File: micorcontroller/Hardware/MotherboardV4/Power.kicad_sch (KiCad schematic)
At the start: 57 parts, among them J0 MS3112E8-4P

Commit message: propper Serial Comand System added
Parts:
- added BuckJmp0: Conn_01x03, Connector_PinHeader_2.54mm:PinHeader_1x03_P2.54mm_Vertical, symbol Connector_Generic:Conn_01x03
- C11: value 12p -> DNP; footprint Capacitor_SMD:C_0805_2012Metric_Pad1.18x1.45mm_HandSolder -> Capacitor_SMD:C_0402_1005Metric_Pad0.74x0.62mm_HandSolder
- C15: value 10u -> DNP
- C18: value 22u -> DNP
- LRlan0, LRre0, LRuC0: footprint SOT230P700X180-4N -> SamacSys_Parts:SOT230P700X180-4N
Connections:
- net +28V: now also BuckJmp0.2 (Pin_2); no longer C12.2, OP0.8 (V+)
- net 3V3_rest: now also C12.2, OP0.8 (V+)
- net GND: now also BuckJmp0.1 (Pin_1)
- net VBuck: now also BuckJmp0.3 (Pin_3)
- net RT: now reaches BUCK0.1 (RT), R11.1
- net SW: now reaches BUCK0.5 (SW), L0.1
- net SW: now also C10.1; no longer C10.2
- net BST: now reaches BUCK0.6 (BST), R14.1
- net SS: now reaches BUCK0.7 (SS), C9.2
- net FB: now reaches BUCK0.8 (FB), C11.2, R15.1, R16.2
- net at R14.2: now also C10.2; no longer C10.1
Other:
- moved on the sheet: C10, C11, C9, L0, R11, R14, R15, R16

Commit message: added a serial command field for easy debugging
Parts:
- removed R1: 12k, Resistor_SMD:R_0603_1608Metric_Pad0.98x0.95mm_HandSolder, symbol Device:R_Small
- added C76, C77: DNP, Capacitor_SMD:C_1210_3225Metric_Pad1.33x2.70mm_HandSolder, symbol Device:C
- C14: value 10u -> 10u/30V
- C17: value 0.1u -> 0.1u/30V
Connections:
- net +28V: now also C76.2
- net GND: now also C76.1, C77.1
- net VBuck: now also C77.2
- net at !bat0.1 (K), R0.1: now also bat0.2 (A)
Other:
- moved on the sheet: BUCK0, BuckJmp0, C10, C11, C13, C14, C15, C16, C17, C18, C9, L0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

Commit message: Switch to header BASED C file system {headache incomming}
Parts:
- removed C18: DNP, Capacitor_SMD:C_0805_2012Metric_Pad1.18x1.45mm_HandSolder, symbol Device:C
- C10: renamed from C76; footprint Capacitor_SMD:C_1210_3225Metric_Pad1.33x2.70mm_HandSolder -> Capacitor_SMD:C_0805_2012Metric_Pad1.18x1.45mm_HandSolder
- C20: renamed from C77; footprint Capacitor_SMD:C_1210_3225Metric_Pad1.33x2.70mm_HandSolder -> Capacitor_SMD:C_0805_2012Metric_Pad1.18x1.45mm_HandSolder
- renumbered C15 to C11, C17 to C12, C9 to C13, C12 to C14, C10 to C15, C11 to C16, C13 to C17, C16 to C18, C14 to C8, C8 to C9, L0 to L1, R2 to R1, R12 to R10, R13 to R12, R14 to R13, R15 to R14, R16 to R15, R3 to R2, R4 to R3, R5 to R4, R6 to R5, R7 to R6, R8 to R7, R9 to R8, R10 to R9
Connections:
- net VBuck renamed VBUCK
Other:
- moved on the sheet: C12, C20

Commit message: startup message
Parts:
- C3: value 0.22uF -> 1u
- C7: value 0.1u -> 1u
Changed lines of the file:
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@@
 			)
 		)
-		(property "Value" "0.1u"
+		(property "Value" "1u"
 			(at 68.58 162.5599 0)
 			(effects
@@
 			)
 		)
-		(property "Value" "0.22uF"
+		(property "Value" "1u"
 			(at 33.274 162.306 0)
 			(effects

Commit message: added uplink
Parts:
- !bat0, 5ext0, 5sys0, bat0, lan0, uC0: symbol Device:LED -> SymbolsBalloonv4:LED
- BT0: symbol Device:Battery_Cell -> SymbolsBalloonv4:Battery_Cell
- BUCK0: symbol SamacSys_Parts:TPS62933DRLR -> SymbolsBalloonv4:TPS62933DRLR
- BuckJmp0, JB_or_U0: symbol Connector_Generic:Conn_01x03 -> SymbolsBalloonv4:Conn_01x03
- C0, C1, C10, C11, C12, C13, C14, C15, C16, C17, C18, C2, C20, C4, C5, C6, C7, C8, C9: symbol Device:C -> SymbolsBalloonv4:C
- C3: value 1u -> 4.7u; symbol Device:C -> SymbolsBalloonv4:C
- D0, D1, D2: symbol Device:D_Zener -> SymbolsBalloonv4:D_Zener
- J0: symbol Connector:DIN-4 -> SymbolsBalloonv4:DIN-4
- L1: symbol Device:L_Small -> SymbolsBalloonv4:L_Small
- LR5V0: symbol SamacSys_Parts:MCP1826S-5002E_DB -> SymbolsBalloonv4:MCP1826S-5002E_DB
- LRlan0, LRre0, LRuC0: symbol SamacSys_Parts:NCP1117ST33T3G -> SymbolsBalloonv4:NCP1117ST33T3G
- OP0: symbol Device:Opamp_Dual -> SymbolsBalloonv4:Opamp_Dual
- R0, R1, R10, R11, R12, R13, R14, R15, R2, R3, R4, R5, R6, R7, R8, R9: symbol Device:R_Small -> SymbolsBalloonv4:R_Small
- R_shunt0: symbol SamacSys_Parts:PA1206FRE7W0R001Z -> SymbolsBalloonv4:PA1206FRE7W0R001Z
- V_BAT0: symbol Connector:Conn_01x04_Socket -> SymbolsBalloonv4:Conn_01x04_Socket

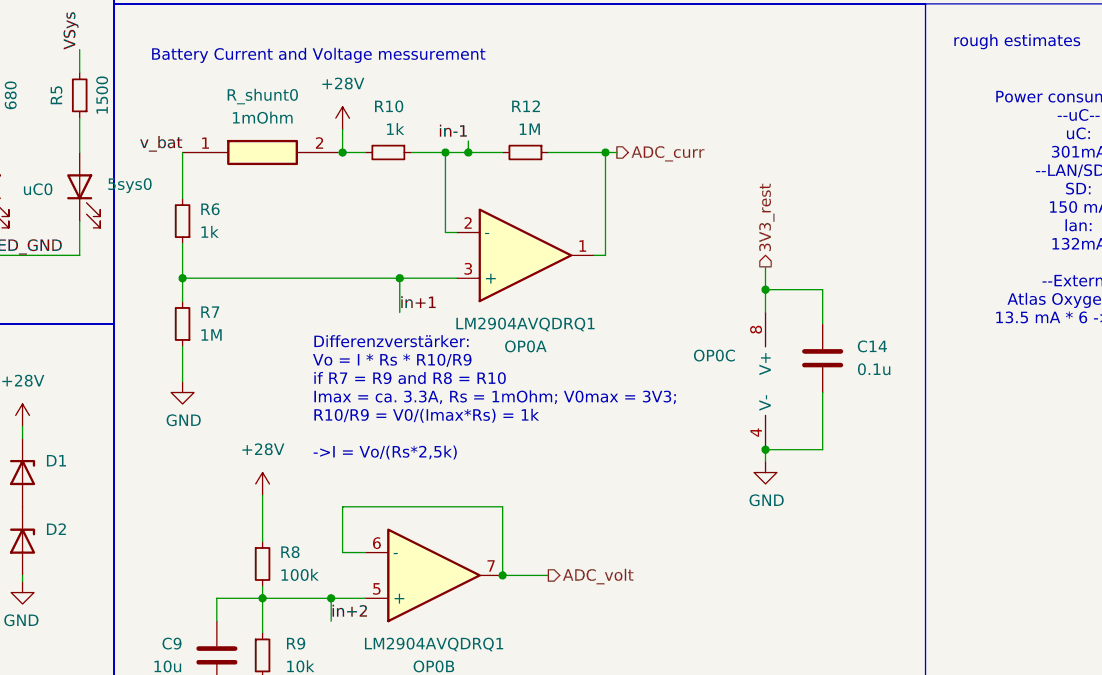
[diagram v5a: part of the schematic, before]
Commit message: changed debug to level based debug and started writing driver for FD-OEM Module
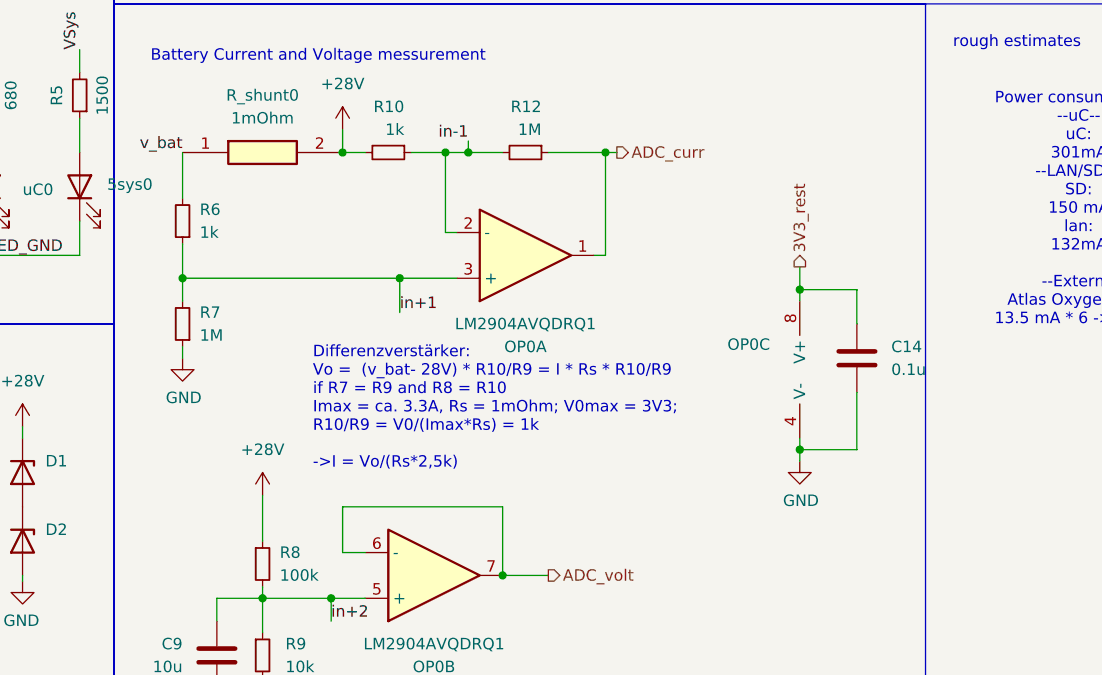
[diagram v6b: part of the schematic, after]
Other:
- note added: "Differenzverstärker: Vo = (v_bat- 28V) * R10/R9 = I * Rs * R10/R9 if R7 = R9 and R8 = R10 Imax = ca. 3.3A, Rs = 1mOhm; V0max = 3V3; R10/R9 = V0/(Imax*Rs) = 1k ->I = Vo/(Rs*2,5k)"
- note removed: "Differenzverstärker: Vo = I * Rs * R10/R9 if R7 = R9 and R8 = R10 Imax = ca. 3.3A, Rs = 1mOhm; V0max = 3V3; R10/R9 = V0/(Imax*Rs) = 1k ->I = Vo/(Rs*2,5k)"
- moved on the sheet: C14, OP0C
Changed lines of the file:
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@@
 	)
 	(junction
-		(at 227.33 129.54)
-		(diameter 0)
-		(color 0 0 0 0)
-	)
-	(junction
 		(at 110.49 125.73)
 		(diameter 0)
@@
 	)
 	(junction
-		(at 227.33 111.76)
-		(diameter 0)
-		(color 0 0 0 0)
-	)
-	(junction
 		(at 48.26 167.64)
 		(diameter 0)
@@
 	)
 	(junction
+		(at 231.14 111.76)
+		(diameter 0)
+		(color 0 0 0 0)
+	)
+	(junction
 		(at 50.8 167.64)
 		(diameter 0)
@@
 	)
 	(junction
+		(at 231.14 129.54)
+		(diameter 0)
+		(color 0 0 0 0)
+	)
+	(junction
 		(at 134.62 138.43)
 		(diameter 0)
@@
 	(wire
 		(pts
-			(xy 227.33 130.81) (xy 227.33 129.54)
+			(xy 231.14 130.81) (xy 231.14 129.54)
 		)
 		(stroke
@@
 	(wire
 		(pts
-			(xy 227.33 111.76) (xy 233.68 111.76)
+			(xy 231.14 111.76) (xy 237.49 111.76)
 		)
 		(stroke
@@
 	(wire
 		(pts
-			(xy 227.33 111.76) (xy 227.33 114.3)
+			(xy 231.14 111.76) (xy 231.14 113.03)
 		)
 		(stroke
@@
 	(wire
 		(pts
-			(xy 227.33 109.22) (xy 227.33 111.76)
+			(xy 231.14 109.22) (xy 231.14 111.76)
 		)
 		(stroke
@@
 	(wire
 		(pts
+			(xy 231.14 128.27) (xy 231.14 129.54)
+		)
+		(stroke
+			(width 0)
+			(type default)
+		)
+	)
+	(wire
+		(pts
 			(xy 105.41 82.55) (xy 105.41 86.36)
 		)
@@
 	(wire
 		(pts
-			(xy 233.68 123.19) (xy 233.68 129.54)
+			(xy 237.49 123.19) (xy 237.49 129.54)
 		)
 		(stroke
@@
 	(wire
 		(pts
-			(xy 233.68 111.76) (xy 233.68 115.57)
+			(xy 237.49 111.76) (xy 237.49 115.57)
 		)
 		(stroke
@@
 	(wire
 		(pts
-			(xy 227.33 129.54) (xy 233.68 129.54)
+			(xy 231.14 129.54) (xy 237.49 129.54)
 		)
 		(stroke
@@
 	(wire
 		(pts
-			(xy 162.56 118.11) (xy 162.56 121.92)
+			(xy 162.56 118.11) (xy 162.56 119.38)
 		)
 		(stroke
@@
 		)
 	)
-	(text "Differenzverstärker:\nVo = I * Rs * R10/R9\nif R7 = R9 and R8 = R10\nImax = ca. 3.3A, Rs = 1mOhm; V0max = 3V3; \nR10/R9 = V0/(Imax*Rs) = 1k\n\n->I = Vo/(Rs*2,5k)\n"
+	(text "Differenzverstärker:\nVo =  (v_bat- 28V) * R10/R9 = I * Rs * R10/R9\nif R7 = R9 and R8 = R10\nImax = ca. 3.3A, Rs = 1mOhm; V0max = 3V3; \nR10/R9 = V0/(Imax*Rs) = 1k\n\n->I = Vo/(Rs*2,5k)\n"
 		(exclude_from_sim no)
-		(at 177.038 130.81 0)
+		(at 177.038 131.826 0)
 		(effects
 			(font
@@
 	(hierarchical_label "3V3_rest"
 		(shape output)
-		(at 227.33 109.22 90)
+		(at 231.14 109.22 90)
 		(fields_autoplaced yes)
 		(effects
@@
 	(symbol
 		(lib_id "SymbolsBalloonv4:Opamp_Dual")
-		(at 229.87 121.92 0)
+		(at 233.68 120.65 0)
 		(unit 3)
 		(exclude_from_sim no)
@@
 		(dnp no)
 		(property "Reference" "OP0"
-			(at 224.028 119.126 0)
+			(at 227.838 117.856 0)
 			(effects
 				(font
@@
 		)
 		(property "Value" "LM2904AVQDRQ1"
-			(at 224.028 121.666 0)
+			(at 227.838 120.396 0)
 			(effects
 				(font
@@
 		)
 		(property "Footprint" "SamacSys_Parts:SOIC127P600X175-8N"
-			(at 229.87 121.92 0)
+			(at 233.68 120.65 0)
 			(effects
 				(font
@@
 		)
 		(property "Datasheet" "~"
-			(at 229.87 121.92 0)
+			(at 233.68 120.65 0)
 			(effects
 				(font
@@
 		)
 		(property "Description" "Dual operational amplifier"
-			(at 229.87 121.92 0)
+			(at 233.68 120.65 0)
 			(effects
 				(font
@@
 		)
 		(property "Sim.Library" "${KICAD7_SYMBOL_DIR}/Simulation_SPICE.sp"
-			(at 229.87 121.92 0)
+			(at 233.68 120.65 0)
 			(effects
 				(font
@@
 		)
 		(property "Sim.Name" "kicad_builtin_opamp_dual"
-			(at 229.87 121.92 0)
+			(at 233.68 120.65 0)
 			(effects
 				(font
@@
 		)
 		(property "Sim.Device" "SUBCKT"
-			(at 229.87 121.92 0)
+			(at 233.68 120.65 0)
 			(effects
 				(font
@@
 		)
 		(property "Sim.Pins" "1=out1 2=in1- 3=in1+ 4=vee 5=in2+ 6=in2- 7=out2 8=vcc"
-			(at 229.87 121.92 0)
+			(at 233.68 120.65 0)
 			(effects
 				(font
@@
 	(symbol
 		(lib_id "SymbolsBalloonv4:C")
-		(at 233.68 119.38 180)
+		(at 237.49 119.38 180)
 		(unit 1)
 		(exclude_from_sim no)
@@
 		(fields_autoplaced yes)
 		(property "Reference" "C14"
-			(at 237.49 118.1099 0)
+			(at 241.3 118.1099 0)
 			(effects
 				(font
@@
 		)
 		(property "Value" "0.1u"
-			(at 237.49 120.6499 0)
+			(at 241.3 120.6499 0)
 			(effects
 				(font
@@
 		)
 		(property "Footprint" "Capacitor_SMD:C_0402_1005Metric_Pad0.74x0.62mm_HandSolder"
-			(at 232.7148 115.57 0)
+			(at 236.5248 115.57 0)
 			(effects
 				(font
@@
 		)
 		(property "Datasheet" "~"
-			(at 233.68 119.38 0)
+			(at 237.49 119.38 0)
 			(effects
 				(font
@@
 		)
 		(property "Description" "Unpolarized capacitor"
-			(at 233.68 119.38 0)
+			(at 237.49 119.38 0)
 			(effects
 				(font
@@
 	(symbol
 		(lib_id "SymbolsBalloonv4:GND")
-		(at 162.56 121.92 0)
+		(at 162.56 119.38 0)
 		(unit 1)
 		(exclude_from_sim no)
@@
 		(dnp no)
 		(property "Reference" "#PWR013"
-			(at 162.56 128.27 0)
+			(at 162.56 125.73 0)
 			(effects
 				(font
@@
 		)
 		(property "Value" "GND"
-			(at 162.687 126.3142 0)
+			(at 162.687 123.7742 0)
 			(effects
 				(font
@@
 		)
 		(property "Footprint" ""
-			(at 162.56 121.92 0)
+			(at 162.56 119.38 0)
 			(effects
 				(font
@@
 		)
 		(property "Datasheet" ""
-			(at 162.56 121.92 0)
+			(at 162.56 119.38 0)
 			(effects
 				(font
@@
 		)
 		(property "Description" "Power symbol creates a global label with name \"GND\" , ground"
-			(at 162.56 121.92 0)
+			(at 162.56 119.38 0)
 			(effects
 				(font
@@
 	(symbol
 		(lib_id "SymbolsBalloonv4:GND")
-		(at 227.33 130.81 0)
+		(at 231.14 130.81 0)
 		(unit 1)
 		(exclude_from_sim no)
@@
 		(dnp no)
 		(property "Reference" "#PWR021"
-			(at 227.33 137.16 0)
+			(at 231.14 137.16 0)
 			(effects
 				(font
@@
 		)
 		(property "Value" "GND"
-			(at 227.457 135.2042 0)
+			(at 231.267 135.2042 0)
 			(effects
 				(font
@@
 		)
 		(property "Footprint" ""
-			(at 227.33 130.81 0)
+			(at 231.14 130.81 0)
 			(effects
 				(font
@@
 		)
 		(property "Datasheet" ""
-			(at 227.33 130.81 0)
+			(at 231.14 130.81 0)
 			(effects
 				(font
@@
 		)
 		(property "Description" "Power symbol creates a global label with name \"GND\" , ground"
-			(at 227.33 130.81 0)
+			(at 231.14 130.81 0)
 			(effects
 				(font
